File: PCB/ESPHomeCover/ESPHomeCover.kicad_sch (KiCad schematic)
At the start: 0 parts

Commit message: Add Board
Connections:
- no-connect marks 3 -> 0
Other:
- sheet Sensors ports: added sen_down, sen_up, sen_win; removed none
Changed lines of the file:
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@@
 	(title_block
 		(title "ESPHome Cover PCB")
-		(date "2024-05-07")
+		(date "2024-05-08")
 		(rev "1")
 	)
-	(no_connect
-		(at 166.37 73.66)
-	)
-	(no_connect
-		(at 166.37 66.04)
-	)
-	(no_connect
-		(at 166.37 69.85)
-	)
 	(wire
 		(pts
@@
 	(wire
 		(pts
+			(xy 166.37 73.66) (xy 208.28 73.66)
+		)
+		(stroke
+			(width 0)
+			(type default)
+		)
+	)
+	(wire
+		(pts
+			(xy 166.37 66.04) (xy 208.28 66.04)
+		)
+		(stroke
+			(width 0)
+			(type default)
+		)
+	)
+	(wire
+		(pts
 			(xy 120.65 68.58) (xy 120.65 128.27)
 		)
@@
 		(pts
 			(xy 120.65 128.27) (xy 80.01 128.27)
+		)
+		(stroke
+			(width 0)
+			(type default)
+		)
+	)
+	(wire
+		(pts
+			(xy 166.37 69.85) (xy 208.28 69.85)
 		)
 		(stroke
@@
 			)
 		)
+		(pin "sen_up" output
+			(at 208.28 66.04 180)
+			(effects
+				(font
+					(size 1.27 1.27)
+				)
+				(justify left)
+			)
+		)
+		(pin "sen_down" output
+			(at 208.28 69.85 180)
+			(effects
+				(font
+					(size 1.27 1.27)
+				)
+				(justify left)
+			)
+		)
+		(pin "sen_win" output
+			(at 208.28 73.66 180)
+			(effects
+				(font
+					(size 1.27 1.27)
+				)
+				(justify left)
+			)
+		)

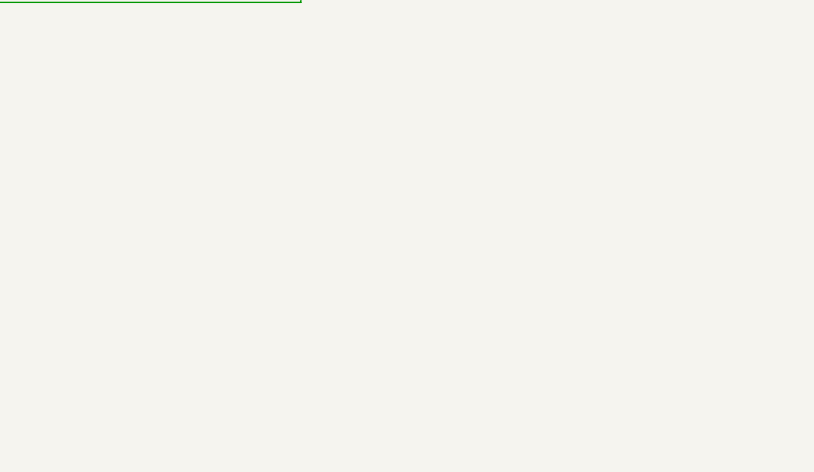
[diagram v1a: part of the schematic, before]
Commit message: small changes
change all Caps to 0603,
add bom
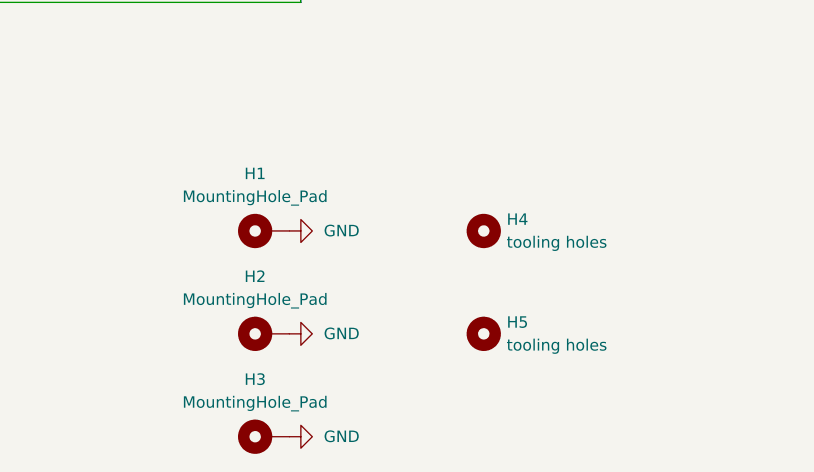
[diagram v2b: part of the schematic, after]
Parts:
- added H1, H2, H3: MountingHole_Pad, MountingHole:MountingHole_3.2mm_M3_ISO14580_Pad, symbol Mechanical:MountingHole_Pad
- added H4, H5: tooling holes, Own_Lib:tooling holes, symbol own lib:toolingholes
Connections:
- new net GND: H1.1, H2.1, H3.1
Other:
- company: (none) -> Tim
